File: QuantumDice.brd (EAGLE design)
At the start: 115.9 x 61.6 mm, 35 parts, among them IC2 LM1117IMPX-3.3, IC3 LM358MX, IC5 MC34063AP

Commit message: PCB updated
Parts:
- removed D1: (no value), diode:SMB
- moved C10 4.83 mm to (52.8, 28.3), turned to 90 degrees
- moved C11 0.47 mm to (56.7, 49.8)
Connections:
- net A_3V renamed A_5V
- net _3V renamed _5V
- removed net VBUS: C11.+, C30.1, C7.+, C8.1, D1.C, F3.2, IC2.3, IC5.6, R25.1
- new net 9V: C11.+, C30.1, C7.+, C8.1, F3.2, IC2.3, IC5.6, R25.1
- net GND: no longer D1.A
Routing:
- net VBUS: track 28.9 -> 0.00 mm
- net 9V: track 0.00 -> 25.5 mm
- net _5V: track 12.0 -> 18.2 mm
- net N$4: track 15.8 -> 20.2 mm
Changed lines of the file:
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@@
 <element name="C8" library="rcl" package="C1206" value="" x="58.1025" y="37.945959375"/>
 <element name="C9" library="rcl" package="C1206" value="" x="63.027559375" y="25.806"/>
-<element name="C10" library="rcl" package="SMC_C" value="" x="52.702459375" y="23.467059375" rot="R270"/>
+<element name="C10" library="rcl" package="SMC_C" value="" x="52.783740625" y="28.298140625" rot="R90"/>
 <element name="IC2" library="lm1117" package="SOT223" value="LM1117IMPX-3.3" x="59.002559375" y="32.1056" rot="R180"/>
 <element name="R18" library="rcl" package="R1206" value="" x="59.002559375" y="24.384" rot="R270"/>
@@
 <element name="IC5" library="mc34063" package="DIL08" value="MC34063AP" x="71.2216" y="48.895" rot="MR270"/>
 <element name="R25" library="rcl" package="R2010" value="0,22/1W" x="62.2808" y="48.895" rot="R90"/>
-<element name="C11" library="rcl" package="SMC_E" value="" x="57.15" y="49.8348" rot="R90"/>
+<element name="C11" library="rcl" package="SMC_E" value="" x="56.682" y="49.8348" rot="R90"/>
 <element name="C25" library="rcl" package="C0603" value="1nF" x="70.5358" y="45.085"/>
 <element name="R26" library="rcl" package="R1206" value="62k5" x="68.834" y="42.799" rot="R180"/>
@@
 <attribute name="PROD_ID" value="CONN-11752" x="63.4492" y="69.5452" size="1.778" layer="27" rot="R270" display="off"/>
 </element>
-<element name="D1" library="diode" package="SMB" value="" x="50.4952" y="46.6848" rot="R180"/>
 <element name="U$5" library="mw" package="GEIGERTUBE" value="STS5" x="11.43" y="4.445"/>
 </elements>
@@
 <wire x1="50.0842" y1="56.6852" x2="50.0842" y2="54.3006" width="0.39878125" layer="1"/>
 <wire x1="50.0842" y1="54.3006" x2="48.6918" y2="52.9082" width="0.39878125" layer="1"/>
-<contactref element="D1" pad="A"/>
 <contactref element="U$5" pad="1B"/>
 <contactref element="U$5" pad="1A"/>
@@
 <wire x1="52.6842" y1="54.329" x2="52.705" y2="54.3082" width="0.39878125" layer="1"/>
 </signal>
-<signal name="VBUS">
+<signal name="9V">
 <contactref element="F3" pad="2"/>
 <contactref element="C7" pad="+"/>
@@
 <contactref element="IC5" pad="6"/>
 <contactref element="C30" pad="1"/>
-<contactref element="D1" pad="C"/>
 <wire x1="67.4116" y1="47.625" x2="69.6858" y2="47.625" width="0.6096" layer="1"/>
 <wire x1="67.4116" y1="47.625" x2="65.405" y2="47.625" width="0.8128" layer="1"/>
 <wire x1="65.405" y1="47.625" x2="64.475" y2="46.695" width="0.8128" layer="1"/>
 <wire x1="62.2808" y1="46.695" x2="64.475" y2="46.695" width="0.8128" layer="1"/>
-<wire x1="52.705" y1="51.5082" x2="52.705" y2="46.6946" width="1.016" layer="1"/>
-<wire x1="52.705" y1="46.6946" x2="52.6952" y2="46.6848" width="1.016" layer="1"/>
-<wire x1="52.705" y1="46.6946" x2="57.1402" y2="46.6946" width="1.4224" layer="1"/>
-<wire x1="57.1402" y1="46.6946" x2="57.15" y2="46.6848" width="1.4224" layer="1"/>
-<wire x1="57.15" y1="46.6848" x2="62.2706" y2="46.6848" width="1.4224" layer="1"/>
+<wire x1="57.1402" y1="46.6946" x2="56.682" y2="46.6848" width="1.4224" layer="1"/>
+<wire x1="56.682" y1="46.6848" x2="62.2706" y2="46.6848" width="1.4224" layer="1"/>
 <wire x1="62.2706" y1="46.6848" x2="62.2808" y2="46.695" width="1.4224" layer="1"/>
 <wire x1="56.6805" y1="35.215659375" x2="56.691559375" y2="35.2046" width="0.8128" layer="1"/>
@@
 <wire x1="56.7025" y1="37.945959375" x2="56.7025" y2="38.0795" width="1.016" layer="1"/>
 <wire x1="56.7025" y1="38.0795" x2="56.682" y2="38.1" width="1.016" layer="1"/>
-<wire x1="56.682" y1="41.7068" x2="57.15" y2="46.6848" width="0" layer="19" extent="1-1"/>
-</signal>
-<signal name="_3V">
+<wire x1="56.682" y1="41.7068" x2="56.682" y2="46.6848" width="1.4224" layer="1"/>
+<wire x1="56.682" y1="46.6848" x2="52.705" y2="51.5082" width="0" layer="19" extent="1-1"/>
+</signal>
+<signal name="_5V">
 <contactref element="C9" pad="1"/>
 <contactref element="C10" pad="+"/>
@@
 <wire x1="59.002559375" y1="29.0066" x2="59.002559375" y2="25.806" width="1.016" layer="1"/>
 <wire x1="59.002559375" y1="25.806" x2="61.627559375" y2="25.806" width="1.016" layer="1"/>
-<wire x1="52.705" y1="25.9696" x2="52.702459375" y2="25.967059375" width="1.27" layer="1"/>
-<wire x1="52.702459375" y1="25.967059375" x2="59.002559375" y2="25.806" width="0" layer="19" extent="1-1"/>
+<wire x1="59.002559375" y1="25.806" x2="52.7916" y2="25.806" width="1.016" layer="1"/>
+<wire x1="52.7916" y1="25.806" x2="52.783740625" y2="25.798140625" width="1.016" layer="1"/>
 </signal>
 <signal name="N$1">
@@
 </polygon>
 </signal>
-<signal name="A_3V">
+<signal name="A_5V">
 <contactref element="R18" pad="2"/>
 <contactref element="C6" pad="1"/>
@@
 <wire x1="65.405" y1="50.165" x2="64.475" y2="51.095" width="0.8128" layer="1"/>
 <wire x1="62.2808" y1="51.095" x2="64.475" y2="51.095" width="0.8128" layer="1"/>
+<wire x1="73.025" y1="55.88" x2="77.47" y2="55.88" width="0.8128" layer="1"/>
 </signal>
 <signal name="N$11">

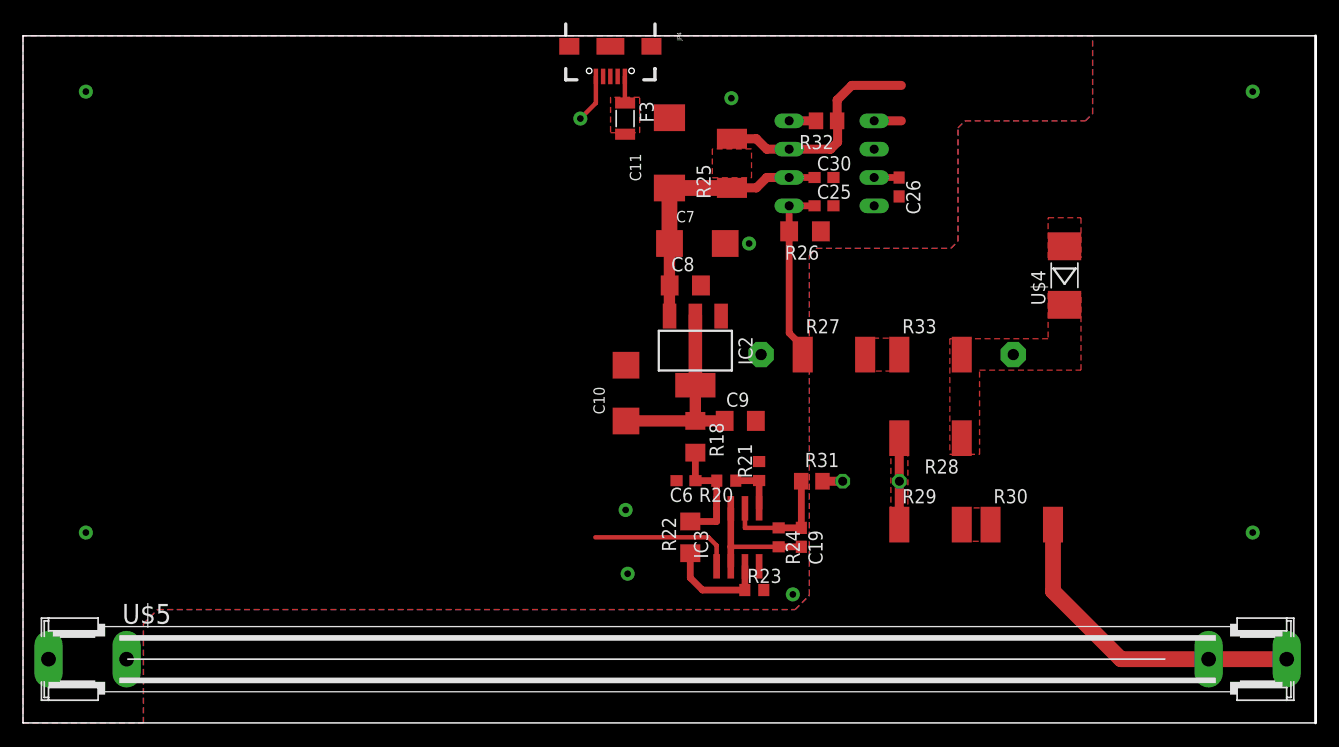
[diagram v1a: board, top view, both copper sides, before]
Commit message: Power circuit updated
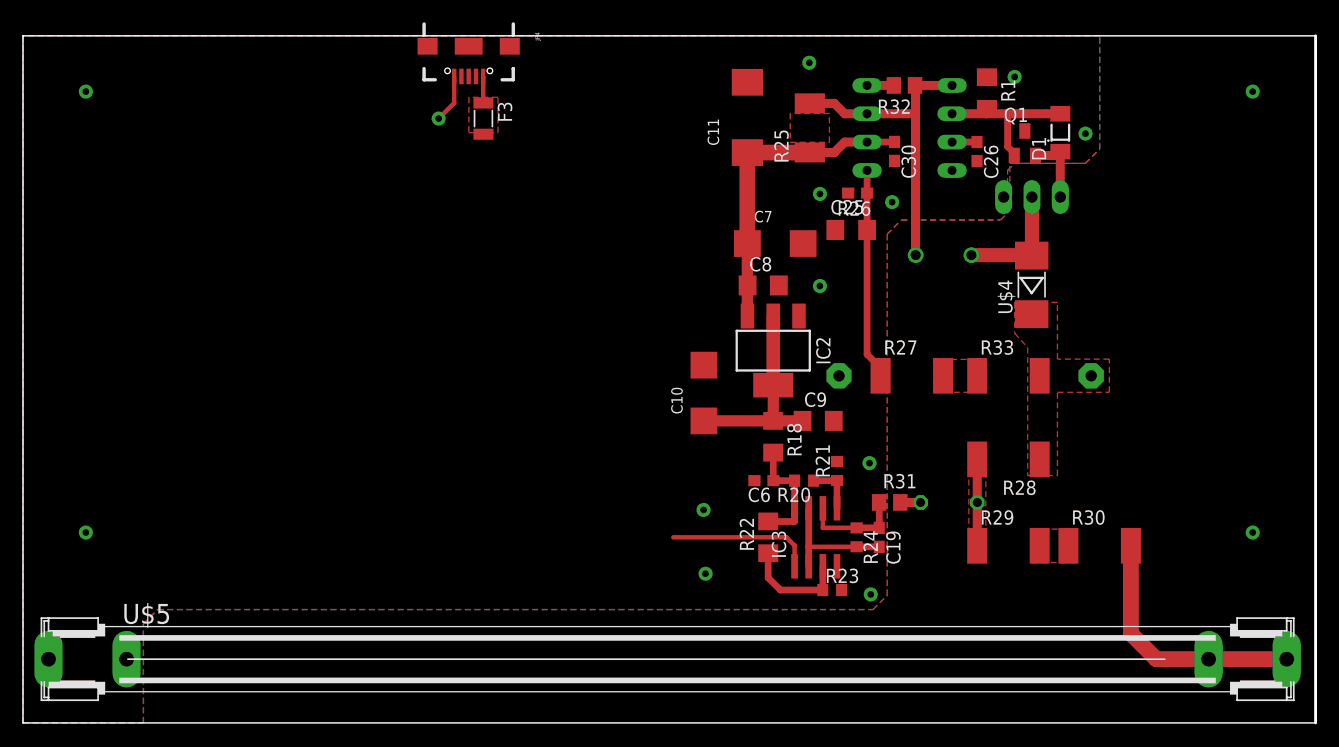
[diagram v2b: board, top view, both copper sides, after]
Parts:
- added D1: LL4148, _hhn_diodes_smd:SOD80_DO213AA_MINIMELF
- added L1: (no value), rcl:6000-XXXX-RC
- added Q1: BC857CSMD, transistor-pnp:SOT23-BEC
- added Q2: 60V/32A/35mΩ, SparkFun-DiscreteSemi:TO220V
- added R1: 470R, rcl:R1206
- moved JP4 12.7 mm to (38.7, 59.4)
- moved F3 12.7 mm to (40.0, 52.9)
- moved C26 7.67 mm to (84.3, 49.9)
- moved R32 7.67 mm to (77.7, 55.9)
- moved C11 7.67 mm to (63.7, 53.0)
- moved IC5 7.67 mm to (78.2, 52.1)
- moved R25 7.67 mm to (69.3, 52.1)
- moved C29 7.24 mm to (83.2, 29.8)
- moved C34 7.24 mm to (81.7, 18.5)
- moved R27 7.24 mm to (78.4, 29.8)
- moved R28 7.24 mm to (87.1, 22.4)
- moved R29 7.24 mm to (87.1, 14.6)
- moved R30 7.24 mm to (95.2, 14.6)
- moved R31 7.24 mm to (76.4, 18.5)
- moved R33 7.24 mm to (87.1, 29.8)
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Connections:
- removed net N$4: IC5.7, R25.2, R32.1
- new net N$2: D1.A, IC5.2, Q1.B, R1.2
- new net N$3: D1.C, Q1.E, Q2.1
- net GND: now also Q1.C, Q2.3, R1.1; no longer IC5.2
- net N$21: now also L1.2, Q2.2
- net N$33: now also IC5.7, L1.1, R25.2, R32.1
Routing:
- net N$33: track 2.44 -> 28.4 mm
- net N$4: track 20.2 -> 0.00 mm
- net N$2: track 0.00 -> 14.1 mm
- net N$21: track 0.00 -> 10.7 mm
- net N$3: track 0.00 -> 6.77 mm
- net N$25: track 29.4 -> 22.8 mm
- net 9V: track 25.5 -> 28.9 mm
- net N$24: track 16.5 -> 19.3 mm
- net N$5: track 11.0 -> 9.08 mm
- net GND: vias 6 -> 11
- removed copper zone on layer 1, net N$21

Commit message: Small updates
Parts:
- removed JP4: USB_MICROB_PLUGCONN-11752, SparkFun-Connectors:USB-B-MICRO-SMD_V03
- added C1, C2, C3, C4: (no value), rcl:C0603
- added IC4: MEGA8-AI, atmel:TQFP32-08
- added J1: AVR_SPI_PRG_6PTH, SparkFun-Connectors:2X3
- added R2: (no value), rcl:R0603
- moved F3 15.9 mm to (55.9, 52.9)
- moved C9 12.2 mm to (67.4, 37.7)
- moved C7 2.54 mm to (66.2, 44.2)
- moved C8 2.54 mm to (65.1, 40.5)
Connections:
- new net MISO: IC4.16, J1.1
- new net MOSI: IC4.15, J1.4
- new net N$6: C4.1, IC4.20
- new net RESET: IC4.29, J1.5, R2.1
- new net SCK: IC4.17, J1.3
- net CPM: now also IC4.32
- net GND: now also C1.2, C2.2, C3.2, C4.2, IC4.21, IC4.3, IC4.5, J1.6; no longer JP4.GND1
- net N$14: no longer JP4.VBUS1
- net _5V: now also C1.1, C2.1, C3.1, IC4.18, IC4.4, IC4.6, J1.2, R2.2
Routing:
- net _5V: track 18.2 -> 67.5 mm, vias 0 -> 1
- net RESET: track 0.00 -> 32.0 mm, vias 0 -> 2
- net SCK: track 0.00 -> 23.9 mm
- net CPM: track 13.1 -> 30.4 mm
- net MISO: track 0.00 -> 16.5 mm
- net MOSI: track 0.00 -> 13.3 mm
- net GND: track 4.35 -> 11.8 mm
- net N$6: track 0.00 -> 3.32 mm
- net N$14: track 2.49 -> 0.13 mm
